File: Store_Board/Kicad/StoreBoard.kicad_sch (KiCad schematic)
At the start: 72 parts, among them J1 Conn_01x10, J2 Conn_01x10, J3 Conn_01x10, J4 Conn_01x10, U1 HM62256BLP, U2 74HCT574, U20 74LS00, U242 74LS32, U3 74HCT574, U4 74HCT04, U417 74LS00, U418 74LS00, U419 74LS08, U420 SN74LS04N, U421 74LS112, U422 SN74LS74, U423 74LS10, U424 74LS32

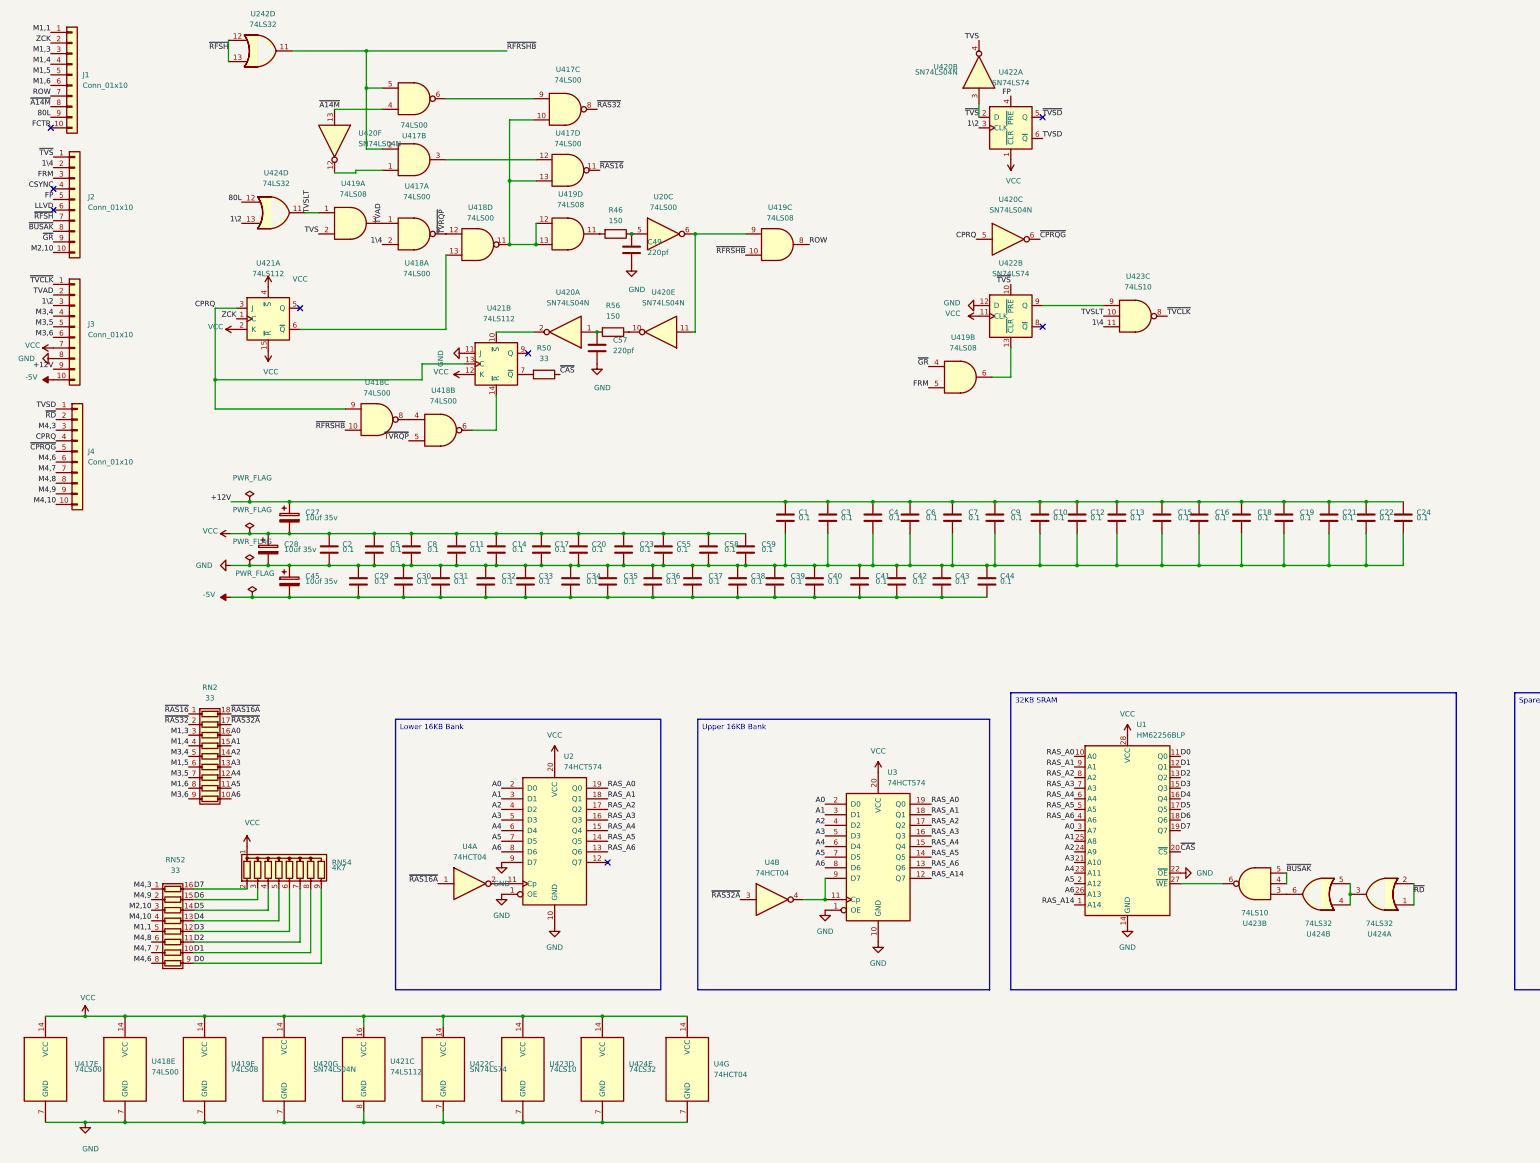
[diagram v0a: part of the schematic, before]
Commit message: Corrections to original schematic
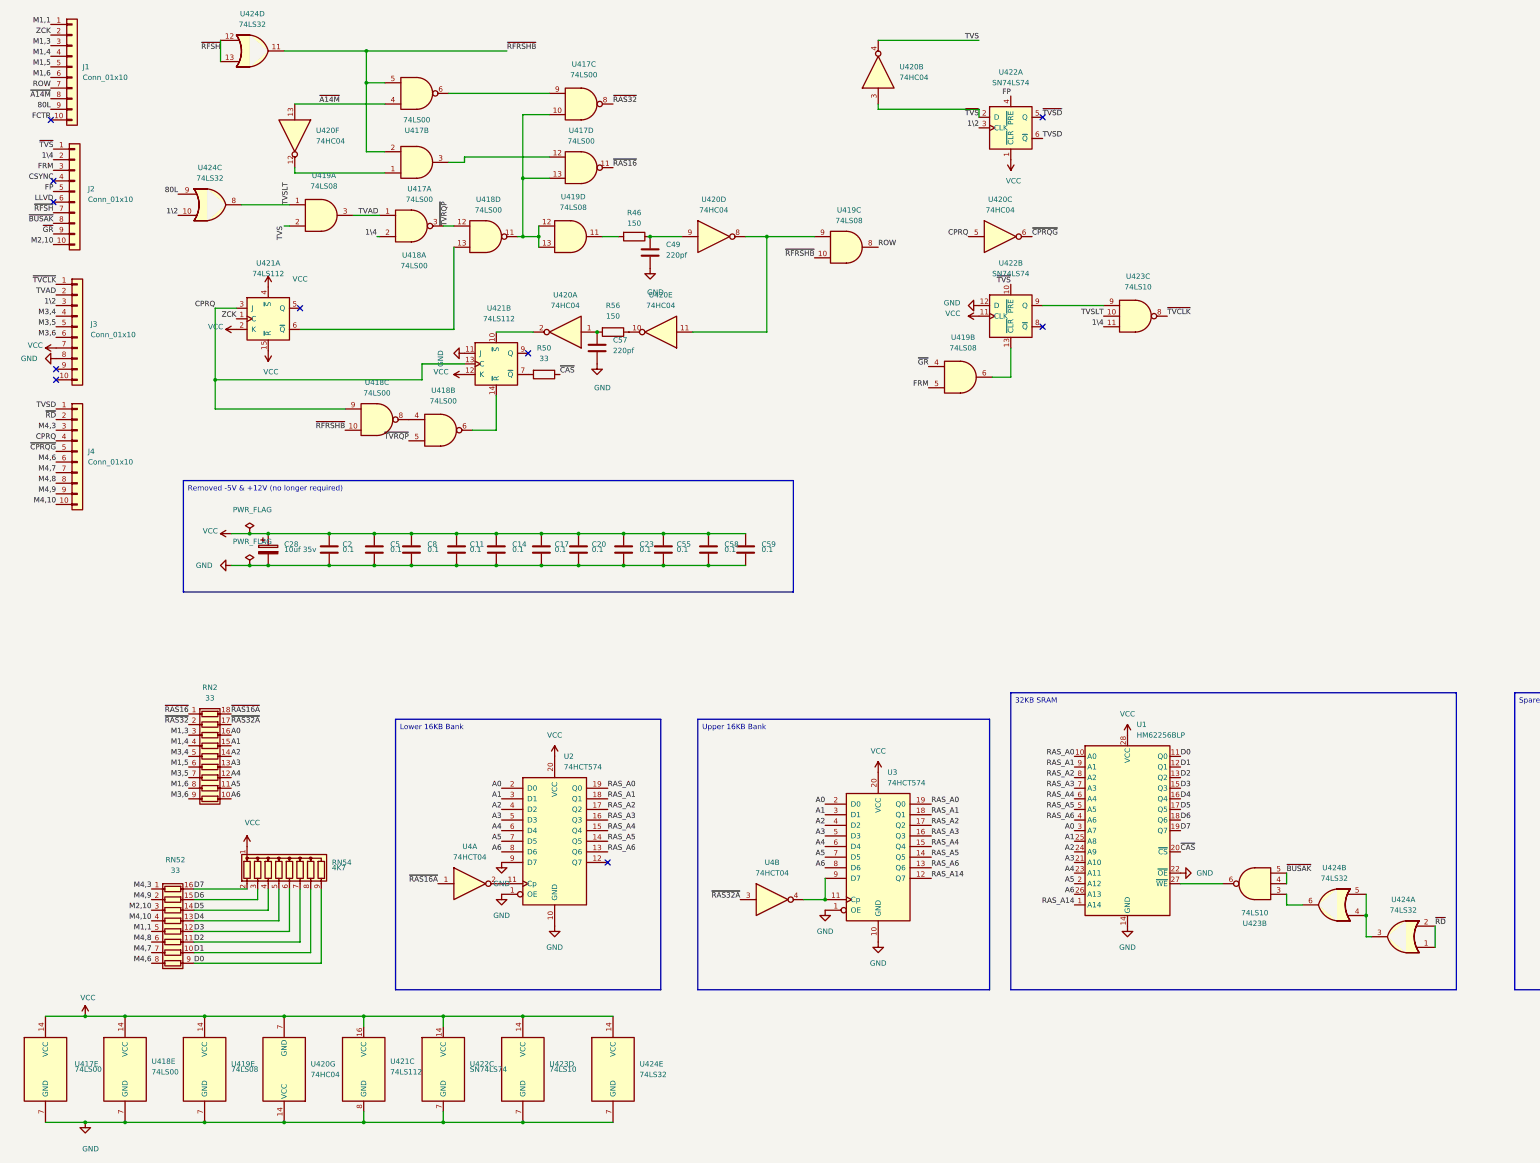
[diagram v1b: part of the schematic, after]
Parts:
- removed C1, C10, C12, C13, C15, C16, C18, C19, C21, C22, C24, C29, C3, C30, C31, C32, C33, C34, C35, C36, C37, C38, C39, C4, C40, C41, C42, C43, C44, C6, C7, C9: 0.1, Capacitor_THT:C_Disc_D3.0mm_W1.6mm_P2.50mm, symbol Device:C
- removed C27, C45: 10uf 35v, Capacitor_THT:CP_Radial_D5.0mm_P2.00mm, symbol NewBrain StoreBoard-rescue:CP-Device
- removed U20: 74LS00, Package_DIP:DIP-16_W7.62mm, symbol 74xx:74LS04
- removed U242: 74LS32, Package_DIP:DIP-16_W7.62mm, symbol 74xx:74LS32
- removed unit 7 of U4
- removed U420: SN74LS04N, Package_DIP:DIP-16_W7.62mm, symbol 74xx:74LS04
- added U420: 74HC04, Package_DIP:DIP-16_W7.62mm, symbol 74xx:74HC04
- added unit 3 of U424
- RN2: footprint (none) -> Package_DIP:DIP-16_W7.62mm
- U2, U3: footprint (none) -> Package_DIP:DIP-20_W7.62mm
- U4: footprint (none) -> Package_DIP:DIP-14_W7.62mm
- U423, U424: footprint Package_DIP:DIP-16_W7.62mm -> Package_DIP:DIP-14_W7.62mm
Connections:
- net 1\2: now also U424.10; no longer U424.13
- net 80L: now also U424.9; no longer U424.12
- net CPRQ: now also U420.5
- net GND: now also U420.14 (VCC)
- net TVS: now also U420.4
- net TVSLT: now also U424.8; no longer U424.11
- net VCC: now also U420.7 (GND)
- net ~{A14M}: now also U420.13
- net ~{CPRQG}: now also U420.6
- net ~{RFRSHB}: now also U424.11
- net ~{RFSH}: now also U424.12, U424.13
- net ~{TVS}: now also U420.3
- net at U417.1: now also U420.12
- net at U421.10 (~{S}): now also U420.2
- net at C57.1, R56.2: now also U420.1
- net at R56.1: now also U420.10
- net at U419.9: now also U420.11, U420.8
- net at C49.1, R46.1: now also U420.9
- net +12V: no longer names the net of J3.9 (Pin_9)
- net -5V: no longer names the net of J3.10 (Pin_10)
- no-connect marks 8 -> 10
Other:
- moved on the sheet: C49, J1, J2, J3, R46, U417A, U417B, U417C, U417D, U418A, U418D, U419A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

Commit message: PCB for testing
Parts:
- RN2: footprint Package_DIP:DIP-16_W7.62mm -> Package_DIP:DIP-18_W7.62mm_Socket
- RN52: footprint Package_DIP:DIP-16_W7.62mm -> Package_DIP:DIP-16_W7.62mm_Socket
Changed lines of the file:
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@@
       (effects (font (size 1.27 1.27)))
     )
-    (property "Footprint" "Package_DIP:DIP-16_W7.62mm" (at 50.8 247.015 90)
+    (property "Footprint" "Package_DIP:DIP-16_W7.62mm_Socket" (at 50.8 247.015 90)
       (effects (font (size 1.27 1.27)) hide)
     )
@@
       (effects (font (size 1.27 1.27)))
     )
-    (property "Footprint" "Package_DIP:DIP-16_W7.62mm" (at 59.69 207.645 90)
-      (effects (font (size 1.27 1.27)) hide)
-    )
+    (property "Footprint" "Package_DIP:DIP-18_W7.62mm_Socket" (at 59.69 207.645 90)
+      (effects (font (size 1.27 1.27)) hide)
+    )

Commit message: Refinements
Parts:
- added HOLE1, HOLE2, HOLE3: HOLE, MountingHole:MountingHole_3.2mm_M3_Pad, symbol my_components:HOLE
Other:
- note added: "Or should we use ~{A14M} signal here?"
- note added: "Use RAS32 to address upper 16KB bank a la A14"
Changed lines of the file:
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@@
     (effects (font (size 1.27 1.27)) (justify left top))
   )
+  (text_box "Mounting Holes"
+    (at 363.22 115.57 0) (size 35.56 34.29)
+    (stroke (width 0) (type default))
+    (fill (type none))
+    (effects (font (size 1.27 1.27)) (justify left top))
+  )
   (text_box "Removed -5V & +12V (no longer required)"
     (at 53.34 127 0) (size 146.05 26.67)
@@
     (effects (font (size 1.27 1.27)) (justify left top))
   )
+  (text "Use RAS32 to address \nupper 16KB bank a la A14" (at 179.07 222.25 0)
+    (effects (font (size 1.27 1.27)) (justify left bottom))
+  )
+  (text "Or should we use \n~{A14M} signal here?" (at 252.8639 235.6016 0)
+    (effects (font (size 1.27 1.27)) (justify left bottom))
+  )
   (label "RAS_A14" (at 266.7 228.6 180) (fields_autoplaced)
     (effects (font (size 1.27 1.27)) (justify right bottom))
@@
   )
   (symbol (lib_id "74xx:74HCT04") (at 194.31 227.33 0) (unit 2)
-    (in_bom yes) (on_board yes) (dnp no) (fields_autoplaced)
-    (property "Reference" "U4" (at 194.31 218.44 0)
+    (in_bom yes) (on_board yes) (dnp no)
+    (property "Reference" "U4" (at 194.31 232.41 0)
       (effects (font (size 1.27 1.27)))
     )
-    (property "Value" "74HCT04" (at 194.31 220.98 0)
+    (property "Value" "74HCT04" (at 194.31 234.95 0)
       (effects (font (size 1.27 1.27)))
     )
@@
     )
   )
+  (symbol (lib_id "my_components:HOLE") (at 379.73 139.7 0) (unit 1)
+    (in_bom yes) (on_board yes) (dnp no) (fields_autoplaced)
+    (property "Reference" "HOLE3" (at 382.27 139.7 0)
+      (effects (font (size 1.524 1.524)) (justify left))
+    )
+    (property "Value" "HOLE" (at 382.27 142.24 0)
+      (effects (font (size 1.524 1.524)) (justify left) hide)
+    )
+    (property "Footprint" "MountingHole:MountingHole_3.2mm_M3_Pad" (at 379.73 139.7 0)
+      (effects (font (size 1.524 1.524)) hide)
+    )
+    (property "Datasheet" "" (at 379.73 139.7 0)
+      (effects (font (size 1.524 1.524)))
+    )
+    (pin "1")
+    (instances
+      (project "StoreBoard"
+        (path "/72d41e3d-fc2f-4390-9c0a-70902589e4df"
+          (reference "HOLE3") (unit 1)
+        )
+      )
+    )
+  )
   (symbol (lib_id "Device:R_Pack09") (at 59.69 193.04 270) (unit 1)
     (in_bom yes) (on_board yes) (dnp no)
@@
     )
   )
+  (symbol (lib_id "my_components:HOLE") (at 379.73 127 0) (unit 1)
+    (in_bom yes) (on_board yes) (dnp no) (fields_autoplaced)
+    (property "Reference" "HOLE1" (at 382.27 127 0)
+      (effects (font (size 1.524 1.524)) (justify left))
+    )
+    (property "Value" "HOLE" (at 382.27 129.54 0)
+      (effects (font (size 1.524 1.524)) (justify left) hide)
+    )
+    (property "Footprint" "MountingHole:MountingHole_3.2mm_M3_Pad" (at 379.73 127 0)
+      (effects (font (size 1.524 1.524)) hide)
+    )
+    (property "Datasheet" "" (at 379.73 127 0)
+      (effects (font (size 1.524 1.524)))
+    )
+    (pin "1")
+    (instances
+      (project "StoreBoard"
+        (path "/72d41e3d-fc2f-4390-9c0a-70902589e4df"
+          (reference "HOLE1") (unit 1)
+        )
+      )
+    )
+  )
   (symbol (lib_id "74xx:74LS32") (at 345.44 236.22 180) (unit 1)
     (in_bom yes) (on_board yes) (dnp no) (fields_autoplaced)
@@
         )
       )
+    )
+  )
+  (symbol (lib_id "my_components:HOLE") (at 379.73 133.35 0) (unit 1)
+    (in_bom yes) (on_board yes) (dnp no) (fields_autoplaced)
+    (property "Reference" "HOLE2" (at 382.27 133.35 0)
+      (effects (font (size 1.524 1.524)) (justify left))
+    )
+    (property "Value" "HOLE" (at 382.27 135.89 0)
+      (effects (font (size 1.524 1.524)) (justify left) hide)
+    )
+    (property "Footprint" "MountingHole:MountingHole_3.2mm_M3_Pad" (at 379.73 133.35 0)
+      (effects (font (size 1.524 1.524)) hide)
+    )
+    (property "Datasheet" "" (at 379.73 133.35 0)
+      (effects (font (size 1.524 1.524)))
+    )
+    (pin "1")
+    (instances
+      (project "StoreBoard"
+        (path "/72d41e3d-fc2f-4390-9c0a-70902589e4df"
+          (reference "HOLE2") (unit 1)
+        )
+      )

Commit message: Update StoreBoard.kicad_sch
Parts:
- renumbered RN2 to RN53
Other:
- moved on the sheet: C11, C14, C17, C2, C20, C23, C28, C49, C5, C55, C57, C58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

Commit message: PCB refinements
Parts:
- removed HOLE3: HOLE, MountingHole:MountingHole_3.2mm_M3_Pad, symbol my_components:HOLE
- R46, R50, R56: footprint Resistor_THT:R_Axial_DIN0204_L3.6mm_D1.6mm_P2.54mm_Vertical -> Resistor_THT:R_Axial_DIN0204_L3.6mm_D1.6mm_P5.08mm_Horizontal
- RN52: footprint Package_DIP:DIP-16_W7.62mm_Socket -> Package_DIP:DIP-16_W7.62mm
- RN53: footprint Package_DIP:DIP-18_W7.62mm_Socket -> Package_DIP:DIP-18_W7.62mm
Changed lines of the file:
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@@
   )
   (text_box "Removed -5V & +12V (no longer required)"
-    (at 96.52 132.08 0) (size 146.05 26.67)
+    (at 96.52 132.08 0) (size 157.48 26.67)
     (stroke (width 0) (type default))
     (fill (type none))
@@
       (effects (font (size 1.27 1.27)))
     )
-    (property "Footprint" "Package_DIP:DIP-16_W7.62mm_Socket" (at 48.26 245.745 90)
+    (property "Footprint" "Package_DIP:DIP-16_W7.62mm" (at 48.26 245.745 90)
       (effects (font (size 1.27 1.27)) hide)
     )
@@
       (effects (font (size 1.27 1.27)))
     )
-    (property "Footprint" "Resistor_THT:R_Axial_DIN0204_L3.6mm_D1.6mm_P2.54mm_Vertical" (at 199.39 68.707 90)
+    (property "Footprint" "Resistor_THT:R_Axial_DIN0204_L3.6mm_D1.6mm_P5.08mm_Horizontal" (at 199.39 68.707 90)
       (effects (font (size 1.27 1.27)) hide)
     )
@@
       (effects (font (size 1.27 1.27)))
     )
-    (property "Footprint" "Resistor_THT:R_Axial_DIN0204_L3.6mm_D1.6mm_P2.54mm_Vertical" (at 194.31 91.567 90)
+    (property "Footprint" "Resistor_THT:R_Axial_DIN0204_L3.6mm_D1.6mm_P5.08mm_Horizontal" (at 194.31 91.567 90)
       (effects (font (size 1.27 1.27)) hide)
     )
@@
       (effects (font (size 1.27 1.27)))
     )
-    (property "Footprint" "Resistor_THT:R_Axial_DIN0204_L3.6mm_D1.6mm_P2.54mm_Vertical" (at 177.8 101.727 90)
+    (property "Footprint" "Resistor_THT:R_Axial_DIN0204_L3.6mm_D1.6mm_P5.08mm_Horizontal" (at 177.8 101.727 90)
       (effects (font (size 1.27 1.27)) hide)
     )
@@
     )
   )
-  (symbol (lib_id "my_components:HOLE") (at 379.73 139.7 0) (unit 1)
-    (in_bom yes) (on_board yes) (dnp no) (fields_autoplaced)
-    (property "Reference" "HOLE3" (at 382.27 139.7 0)
-      (effects (font (size 1.524 1.524)) (justify left))
-    )
-    (property "Value" "HOLE" (at 382.27 142.24 0)
-      (effects (font (size 1.524 1.524)) (justify left) hide)
-    )
-    (property "Footprint" "MountingHole:MountingHole_3.2mm_M3_Pad" (at 379.73 139.7 0)
-      (effects (font (size 1.524 1.524)) hide)
-    )
-    (property "Datasheet" "" (at 379.73 139.7 0)
-      (effects (font (size 1.524 1.524)))
-    )
-    (pin "1")
-    (instances
-      (project "StoreBoard"
-        (path "/72d41e3d-fc2f-4390-9c0a-70902589e4df"
-          (reference "HOLE3") (unit 1)
-        )
-      )
-    )
-  )
   (symbol (lib_id "Device:R_Pack09") (at 54.61 184.15 270) (unit 1)
     (in_bom yes) (on_board yes) (dnp no)
@@
       (effects (font (size 1.27 1.27)))
     )
-    (property "Footprint" "Package_DIP:DIP-18_W7.62mm_Socket" (at 54.61 198.755 90)
-      (effects (font (size 1.27 1.27)) hide)
-    )
+    (property "Footprint" "Package_DIP:DIP-18_W7.62mm" (at 54.61 198.755 90)
+      (effects (font (size 1.27 1.27)) hide)
+    )

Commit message: Refinements
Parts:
- added TP1: TP_A14M, TestPoint:TestPoint_THTPad_D2.0mm_Drill1.0mm, symbol Connector_Generic:Conn_01x01
- added TP2: TP_~{CAS}, TestPoint:TestPoint_THTPad_D2.0mm_Drill1.0mm, symbol Connector_Generic:Conn_01x01
- added TP3: TP_RAS16A, TestPoint:TestPoint_THTPad_D2.0mm_Drill1.0mm, symbol Connector_Generic:Conn_01x01
- added TP4: TP_RAS32A, TestPoint:TestPoint_THTPad_D2.0mm_Drill1.0mm, symbol Connector_Generic:Conn_01x01
- C11, C14, C17, C2, C20, C23, C5, C55, C58, C59, C8: value 0.1 -> 100nF
- C28: value 10uf 35v -> 110µF 35v
- C49, C57: value 220pf -> 220pF
- R46, R56: value 150 -> 150Ω
- R50, RN52, RN53: value 33 -> 33Ω
- RN54: value 4K7 -> 4.7KΩ
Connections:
- net GND: now also HOLE1.1, HOLE2.1
- net ~{CAS}: now also TP2.1 (Pin_1)
- net A14M: now reaches U417.1, U420.12
- net A14M: now also TP1.1 (Pin_1)
- net RAS32A: now reaches U3.11 (Cp), U3.9 (D7), U4.4
- net RAS32A: now also TP4.1 (Pin_1)
- net RAS16A: now reaches U2.11 (Cp), U4.2
- net RAS16A: now also TP3.1 (Pin_1)
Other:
- moved on the sheet: J1, J2, J3, J4, RN52, RN53, RN54, U1, U2, U3, U417E, U418E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
